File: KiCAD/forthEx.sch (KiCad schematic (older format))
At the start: 58 parts, among them CON1 SD_Card, CON2 BARREL_JACK 2,1mm, J1 RCA_JACK, J2 RCA_JACK, J3 RJ12, P1 ICSP, Q1 2N3906, Q2 2N3904, SW1 Power, SW2 reset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

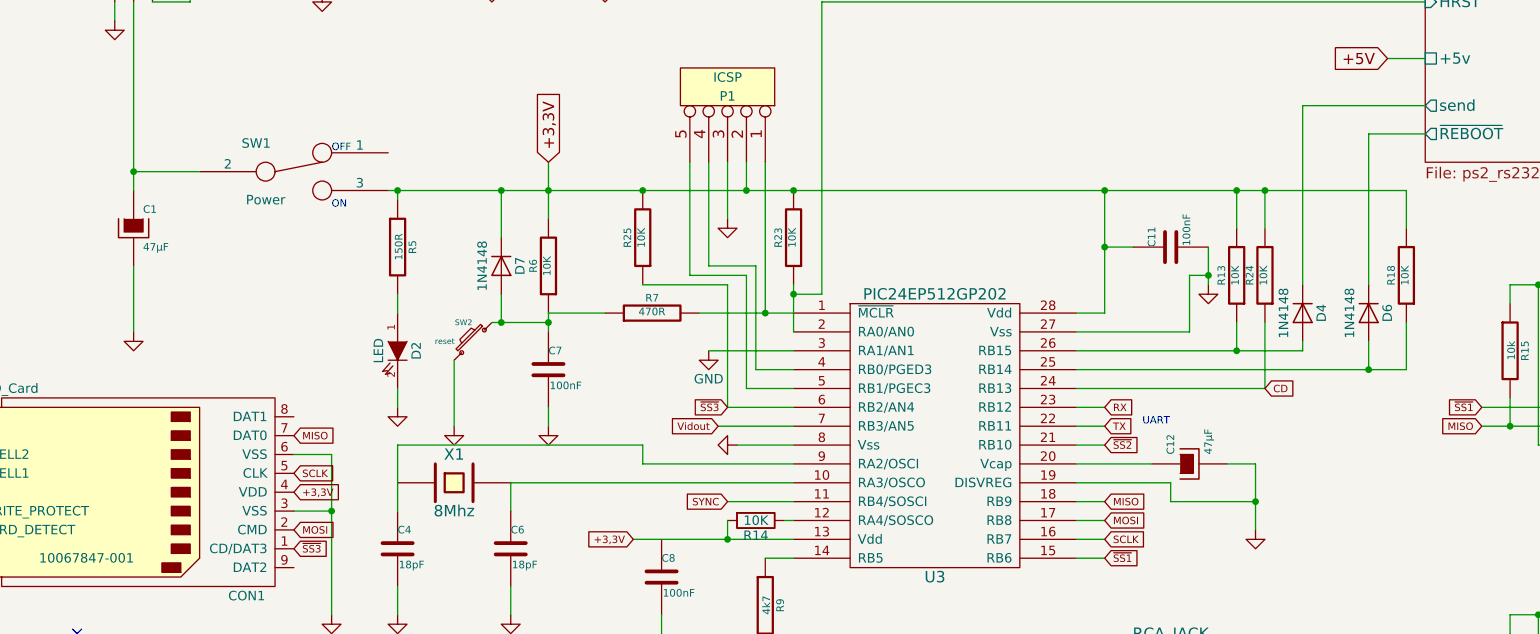
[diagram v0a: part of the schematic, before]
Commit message: Mise à jour schématique Modification à BOOT, protection contre les images passées date. Lorsque le système est mis à jour les images sauvegardées avant cette mise à jour sont invalides.
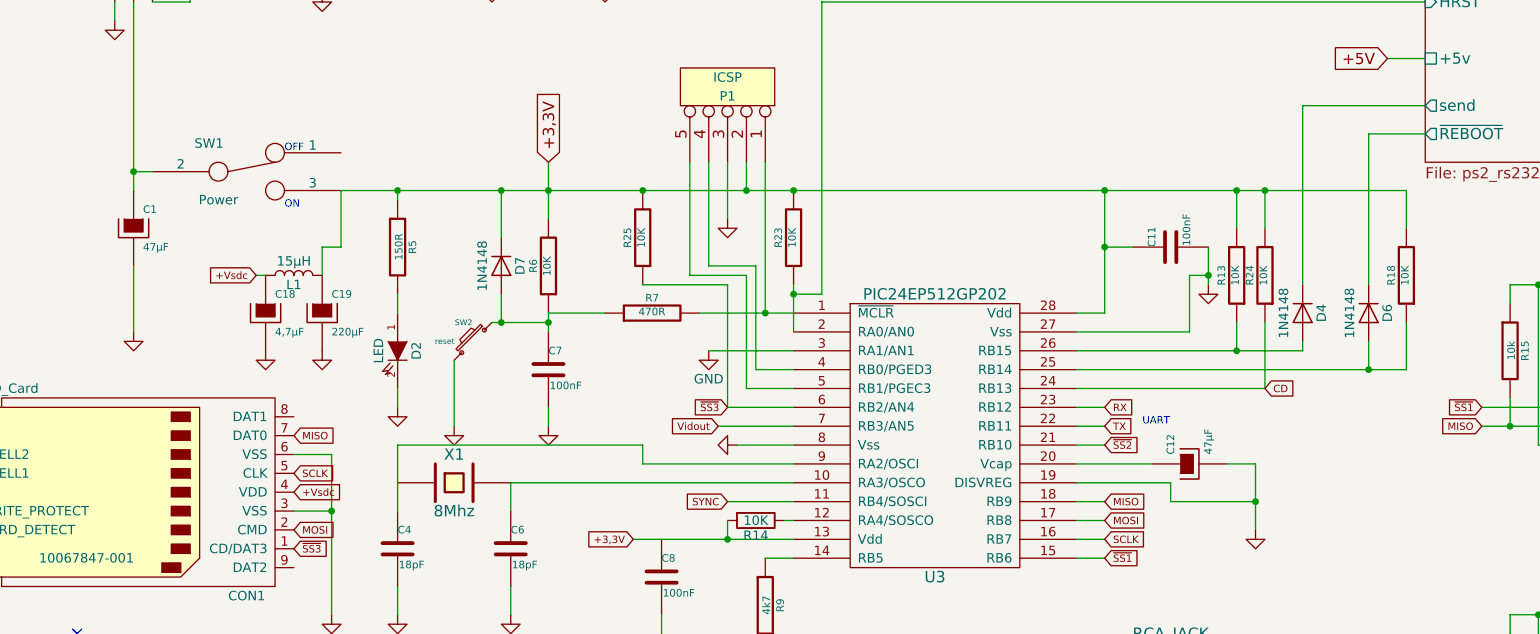
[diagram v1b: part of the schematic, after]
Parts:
- added C18: 4,7µF, ~, symbol CAPAPOL
- added C19: 220µF, ~, symbol CAPAPOL
- added L1: 15µH, symbol L
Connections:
- net +3,3V: now also C19.1, L1.2; no longer CON1.4 (VDD)
- net GND: now also C18.2, C19.2
- new net +Vsdc: C18.1, CON1.4 (VDD), L1.1
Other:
- moved on the sheet: SW1
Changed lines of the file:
@@
 $EndComp
 $Comp
-L GND #PWR23
+L GND #PWR25
 U 1 1 55772493
 P 6300 5700
-F 0 "#PWR23" H 6300 5700 30  0001 C CNN
+F 0 "#PWR25" H 6300 5700 30  0001 C CNN
 F 1 "GND" H 6300 5630 30  0001 C CNN
 F 2 "" H 6300 5700 60  0000 C CNN
@@
 $EndComp
 $Comp
-L GND #PWR22
+L GND #PWR24
 U 1 1 5577274E
 P 5950 7450
-F 0 "#PWR22" H 5950 7450 30  0001 C CNN
+F 0 "#PWR24" H 5950 7450 30  0001 C CNN
 F 1 "GND" H 5950 7380 30  0001 C CNN
 F 2 "" H 5950 7450 60  0000 C CNN
@@
 $EndComp
 $Comp
-L GND #PWR14
+L GND #PWR16
 U 1 1 55772AE7
 P 3900 3650
-F 0 "#PWR14" H 3900 3650 30  0001 C CNN
+F 0 "#PWR16" H 3900 3650 30  0001 C CNN
 F 1 "GND" H 3900 3580 30  0001 C CNN
 F 2 "" H 3900 3650 60  0000 C CNN
@@
 $EndComp
 $Comp
-L GND #PWR11
+L GND #PWR13
 U 1 1 55772AF4
 P 3400 3650
-F 0 "#PWR11" H 3400 3650 30  0001 C CNN
+F 0 "#PWR13" H 3400 3650 30  0001 C CNN
 F 1 "GND" H 3400 3580 30  0001 C CNN
 F 2 "" H 3400 3650 60  0000 C CNN
@@
 $EndComp
 $Comp
-L GND #PWR18
+L GND #PWR20
 U 1 1 55772BB1
 P 4850 2550
-F 0 "#PWR18" H 4850 2550 30  0001 C CNN
+F 0 "#PWR20" H 4850 2550 30  0001 C CNN
 F 1 "GND" H 4850 2480 30  0001 C CNN
 F 2 "" H 4850 2550 60  0000 C CNN
@@
 $EndComp
 $Comp
-L GND #PWR25
+L GND #PWR27
 U 1 1 55772ED2
 P 7400 2900
-F 0 "#PWR25" H 7400 2900 30  0001 C CNN
+F 0 "#PWR27" H 7400 2900 30  0001 C CNN
 F 1 "GND" H 7400 2830 30  0001 C CNN
 F 2 "" H 7400 2900 60  0000 C CNN
@@
 $EndComp
 $Comp
-L GND #PWR16
+L GND #PWR18
 U 1 1 55772F91
 P 4500 4750
-F 0 "#PWR16" H 4500 4750 30  0001 C CNN
+F 0 "#PWR18" H 4500 4750 30  0001 C CNN
 F 1 "GND" H 4500 4680 30  0001 C CNN
 F 2 "" H 4500 4750 60  0000 C CNN
@@
 $EndComp
 $Comp
-L GND #PWR26
+L GND #PWR28
 U 1 1 55773073
 P 7650 4200
-F 0 "#PWR26" H 7650 4200 30  0001 C CNN
+F 0 "#PWR28" H 7650 4200 30  0001 C CNN
 F 1 "GND" H 7650 4130 30  0001 C CNN
 F 2 "" H 7650 4200 60  0000 C CNN
@@
 $EndComp
 $Comp
-L GND #PWR13
+L GND #PWR15
 U 1 1 55773799
 P 3700 4650
-F 0 "#PWR13" H 3700 4650 30  0001 C CNN
+F 0 "#PWR15" H 3700 4650 30  0001 C CNN
 F 1 "GND" H 3700 4580 30  0001 C CNN
 F 2 "" H 3700 4650 60  0000 C CNN
@@
 $EndComp
 $Comp
-L GND #PWR9
+L GND #PWR11
 U 1 1 5577379F
 P 3100 4650
-F 0 "#PWR9" H 3100 4650 30  0001 C CNN
+F 0 "#PWR11" H 3100 4650 30  0001 C CNN
 F 1 "GND" H 3100 4580 30  0001 C CNN
 F 2 "" H 3100 4650 60  0000 C CNN
@@
 $EndComp
 $Comp
-L GND #PWR27
+L GND #PWR29
 U 1 1 55773979
 P 9350 4050
-F 0 "#PWR27" H 9350 4050 30  0001 C CNN
+F 0 "#PWR29" H 9350 4050 30  0001 C CNN
 F 1 "GND" H 9350 3980 30  0001 C CNN
 F 2 "" H 9350 4050 60  0000 C CNN
@@
 $EndComp
 $Comp
-L GND #PWR29
+L GND #PWR31
 U 1 1 55773B44
 P 10900 3700
-F 0 "#PWR29" H 10900 3700 30  0001 C CNN
+F 0 "#PWR31" H 10900 3700 30  0001 C CNN
 F 1 "GND" H 10900 3630 30  0001 C CNN
 F 2 "" H 10900 3700 60  0000 C CNN
@@
 L SWITCH_INV SW1
 U 1 1 55775625
-P 2550 2300
-F 0 "SW1" H 2350 2450 50  0000 C CNN
-F 1 "Power" H 2400 2150 50  0000 C CNN
-F 2 "~" H 2550 2300 60  0000 C CNN
-F 3 "~" H 2550 2300 60  0000 C CNN
-	1    2550 2300
-	1    0    0    -1
-$EndComp
-$Comp
-L GND #PWR3
+P 2300 2300
+F 0 "SW1" H 2100 2450 50  0000 C CNN
+F 1 "Power" H 2150 2150 50  0000 C CNN
+F 2 "~" H 2300 2300 60  0000 C CNN
+F 3 "~" H 2300 2300 60  0000 C CNN
+	1    2300 2300
+	1    0    0    -1
+$EndComp
+$Comp
+L GND #PWR5
 U 1 1 55775634
 P 1700 3150
-F 0 "#PWR3" H 1700 3150 30  0001 C CNN
+F 0 "#PWR5" H 1700 3150 30  0001 C CNN
 F 1 "GND" H 1700 3080 30  0001 C CNN
 F 2 "" H 1700 3150 60  0000 C CNN
@@
 $EndComp
 $Comp
-L GND #PWR19
+L GND #PWR21
 U 1 1 557795A1
 P 4900 3750
-F 0 "#PWR19" H 4900 3750 30  0001 C CNN
+F 0 "#PWR21" H 4900 3750 30  0001 C CNN
 F 1 "GND" H 4900 3680 30  0001 C CNN
 F 2 "" H 4900 3750 60  0000 C CNN
@@
 $EndComp
 $Comp
-L GND #PWR8
+L GND #PWR10
 U 1 1 557C9D8C
 P 3100 3550
-F 0 "#PWR8" H 3100 3550 30  0001 C CNN
+F 0 "#PWR10" H 3100 3550 30  0001 C CNN
 F 1 "GND" H 3100 3480 30  0001 C CNN
 F 2 "" H 3100 3550 60  0000 C CNN
@@
 $EndComp
 $Comp
-L GND #PWR2
+L GND #PWR4
 U 1 1 557CC219
 P 1600 1500
-F 0 "#PWR2" H 1600 1500 30  0001 C CNN
+F 0 "#PWR4" H 1600 1500 30  0001 C CNN
 F 1 "GND" H 1600 1430 30  0001 C CNN
 F 2 "" H 1600 1500 60  0000 C CNN
@@
 $EndComp
 $Comp
-L GND #PWR15
+L GND #PWR17
 U 1 1 557CC2EB
 P 4200 1300
-F 0 "#PWR15" H 4200 1300 30  0001 C CNN
+F 0 "#PWR17" H 4200 1300 30  0001 C CNN
 F 1 "GND" H 4200 1230 30  0001 C CNN
 F 2 "" H 4200 1300 60  0000 C CNN
@@
 	1    0    0    -1
 $EndComp
-Text Notes 2750 2500 0    39   ~ 0
+Text Notes 2500 2500 0    39   ~ 0
 ON
-Text Notes 2750 2200 0    39   ~ 0
+Text Notes 2500 2200 0    39   ~ 0
 OFF
 $Comp
@@
 $EndComp
 $Comp
-L GND #PWR24
+L GND #PWR26
 U 1 1 557CD0FD
 P 7200 5650
-F 0 "#PWR24" H 7200 5650 30  0001 C CNN
+F 0 "#PWR26" H 7200 5650 30  0001 C CNN
 F 1 "GND" H 7200 5580 30  0001 C CNN
 F 2 "" H 7200 5650 60  0000 C CNN
@@
 Vidout
 $Comp
-L GND #PWR28
+L GND #PWR30
 U 1 1 55FA1459
 P 9350 5800
-F 0 "#PWR28" H 9350 5800 30  0001 C CNN
+F 0 "#PWR30" H 9350 5800 30  0001 C CNN
 F 1 "GND" H 9350 5730 30  0001 C CNN
 F 2 "" H 9350 5800 60  0000 C CNN
@@
 $EndComp
 $Comp
-L GND #PWR30
+L GND #PWR32
 U 1 1 55FA1465
 P 10900 5450
-F 0 "#PWR30" H 10900 5450 30  0001 C CNN
+F 0 "#PWR32" H 10900 5450 30  0001 C CNN
 F 1 "GND" H 10900 5380 30  0001 C CNN
 F 2 "" H 10900 5450 60  0000 C CNN
@@
 ~SS2
 $Comp
-L GND #PWR5
+L GND #PWR7
 U 1 1 5600DB37
 P 2700 1350
-F 0 "#PWR5" H 2700 1350 30  0001 C CNN
+F 0 "#PWR7" H 2700 1350 30  0001 C CNN
 F 1 "GND" H 2700 1280 30  0001 C CNN
 F 2 "" H 2700 1350 60  0000 C CNN
@@
 $EndComp
 $Comp
-L GND #PWR21
+L GND #PWR23
 U 1 1 56014C24
 P 5950 5500
-F 0 "#PWR21" H 5950 5500 30  0001 C CNN
+F 0 "#PWR23" H 5950 5500 30  0001 C CNN
 F 1 "GND" H 5950 5430 30  0001 C CNN
 F 2 "" H 5950 5500 60  0000 C CNN
@@
 $EndComp
 $Comp
-L GND #PWR20
+L GND #PWR22
 U 1 1 56014C57
 P 5050 5500
-F 0 "#PWR20" H 5050 5500 30  0001 C CNN
+F 0 "#PWR22" H 5050 5500 30  0001 C CNN
 F 1 "GND" H 5050 5430 30  0001 C CNN
 F 2 "" H 5050 5500 60  0000 C CNN
@@
 $EndComp
 $Comp
-L GND #PWR7
+L GND #PWR9
 U 1 1 5613F3E7
 P 3050 7050
-F 0 "#PWR7" H 3050 7050 30  0001 C CNN
+F 0 "#PWR9" H 3050 7050 30  0001 C CNN
 F 1 "GND" H 3050 6980 30  0001 C CNN
 F 2 "" H 3050 7050 60  0000 C CNN
@@
 $EndComp
 $Comp
-L GND #PWR4
+L GND #PWR6
 U 1 1 5613F601
 P 1850 7400
-F 0 "#PWR4" H 1850 7400 30  0001 C CNN
+F 0 "#PWR6" H 1850 7400 30  0001 C CNN
 F 1 "GND" H 1850 7330 30  0001 C CNN
 F 2 "" H 1850 7400 60  0000 C CNN
@@
 $EndComp
 $Comp
-L GND #PWR10
+L GND #PWR12
 U 1 1 5808AF37
 P 3200 1250
-F 0 "#PWR10" H 3200 1250 30  0001 C CNN
+F 0 "#PWR12" H 3200 1250 30  0001 C CNN
 F 1 "GND" H 3200 1180 30  0001 C CNN
 F 2 "" H 3200 1250 60  0000 C CNN
@@
 CD
 $Comp
-L GND #PWR6
+L GND #PWR8
 U 1 1 5808F945
 P 2750 4650
-F 0 "#PWR6" H 2750 4650 30  0001 C CNN
+F 0 "#PWR8" H 2750 4650 30  0001 C CNN
 F 1 "GND" H 2750 4580 30  0001 C CNN
 F 2 "" H 2750 4650 60  0000 C CNN
@@
 $EndComp
 Text GLabel 2550 4000 2    39   Input ~ 0
-+3,3V
++Vsdc
 Text GLabel 4850 3550 0    39   Input ~ 0
 ~SS3
@@
 $EndComp
 $Comp
-L GND #PWR12
+L GND #PWR14
 U 1 1 5807E91E
 P 3600 1300
-F 0 "#PWR12" H 3600 1300 30  0001 C CNN
+F 0 "#PWR14" H 3600 1300 30  0001 C CNN
 F 1 "GND" H 3600 1230 30  0001 C CNN
 F 2 "" H 3600 1300 60  0000 C CNN
@@
 $EndComp
 $Comp
-L GND #PWR1
+L GND #PWR2
 U 1 1 5873C0B4
 P 1150 6050
-F 0 "#PWR1" H 1150 5800 50  0001 C CNN
+F 0 "#PWR2" H 1150 5800 50  0001 C CNN
 F 1 "GND" H 1150 5900 50  0000 C CNN
 F 2 "" H 1150 6050 50  0000 C CNN
@@
 	1700 1400 1700 2400
 Wire Wire Line
-	1700 2300 2050 2300
-Wire Wire Line
 	7200 4050 7650 4050
 Wire Wire Line
@@
 	8350 1700 8550 1700
 Wire Wire Line
-	3050 2400 8450 2400
+	2800 2400 8450 2400
 Wire Wire Line
 	7900 3250 7900 3200
@@
 	5150 4150 5200 4150
 $Comp
-L GND #PWR17
+L GND #PWR19
 U 1 1 5873EFC8
 P 4750 3250
-F 0 "#PWR17" H 4750 3000 50  0001 C CNN
+F 0 "#PWR19" H 4750 3000 50  0001 C CNN
 F 1 "GND" H 4750 3100 50  0000 C CNN
 F 2 "" H 4750 3250 50  0000 C CNN
@@
 	8450 3350 8450 3100
 Connection ~ 8250 3350
+$Comp
+L L L1
+U 1 1 58E82954
+P 2550 2850
+F 0 "L1" V 2500 2850 50  0000 C CNN
+F 1 "15µH" V 2625 2850 50  0000 C CNN
+F 2 "" H 2550 2850 50  0001 C CNN
+F 3 "" H 2550 2850 50  0001 C CNN
+	1    2550 2850
+	0    -1   -1   0
+$EndComp
+$Comp
+L CAPAPOL C18
+U 1 1 58E84A23
+P 2400 3050
+F 0 "C18" H 2450 3150 40  0000 L CNN
+F 1 "4,7µF" H 2450 2950 40  0000 L CNN
+F 2 "~" H 2500 2900 30  0000 C CNN
+F 3 "~" H 2400 3050 300 0000 C CNN
+	1    2400 3050
+	1    0    0    -1
+$EndComp
+$Comp
+L CAPAPOL C19
+U 1 1 58E84B29
+P 2700 3050
+F 0 "C19" H 2750 3150 40  0000 L CNN
+F 1 "220µF" H 2750 2950 40  0000 L CNN
+F 2 "~" H 2800 2900 30  0000 C CNN
+F 3 "~" H 2700 3050 300 0000 C CNN
+	1    2700 3050
+	1    0    0    -1
+$EndComp
+$Comp
+L GND #PWR1
+U 1 1 58E84D59
+P 2400 3250
+F 0 "#PWR1" H 2400 3250 30  0001 C CNN
+F 1 "GND" H 2400 3180 30  0001 C CNN
+F 2 "" H 2400 3250 60  0000 C CNN
+F 3 "" H 2400 3250 60  0000 C CNN
+	1    2400 3250
+	1    0    0    -1
+$EndComp
+$Comp
+L GND #PWR3
+U 1 1 58E84FE5
+P 2700 3250
+F 0 "#PWR3" H 2700 3250 30  0001 C CNN
+F 1 "GND" H 2700 3180 30  0001 C CNN
+F 2 "" H 2700 3250 60  0000 C CNN
+F 3 "" H 2700 3250 60  0000 C CNN
+	1    2700 3250
+	1    0    0    -1
+$EndComp
+Text GLabel 2350 2850 0    39   Input ~ 0
++Vsdc
+Wire Wire Line
+	2350 2850 2400 2850
+Wire Wire Line
+	2700 2850 2700 2700
+Wire Wire Line
+	1700 2300 1800 2300
+Wire Wire Line
+	2700 2700 2800 2700
+Wire Wire Line
+	2800 2700 2800 2400
 $EndSCHEMATC

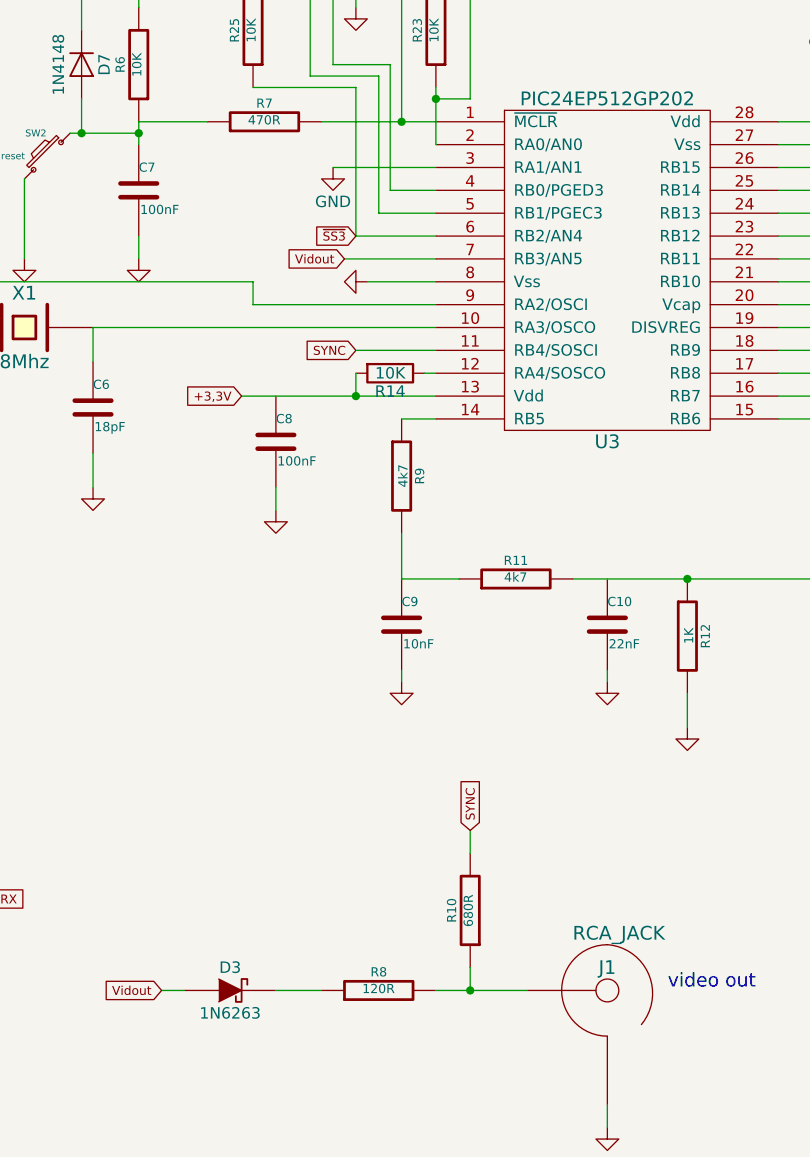
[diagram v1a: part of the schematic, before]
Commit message: Modification au générateur vidéo pour ajouter un seuil noir en utilisant OC4.
Création et travail sur block.s
Retiré eefs.s du projet.
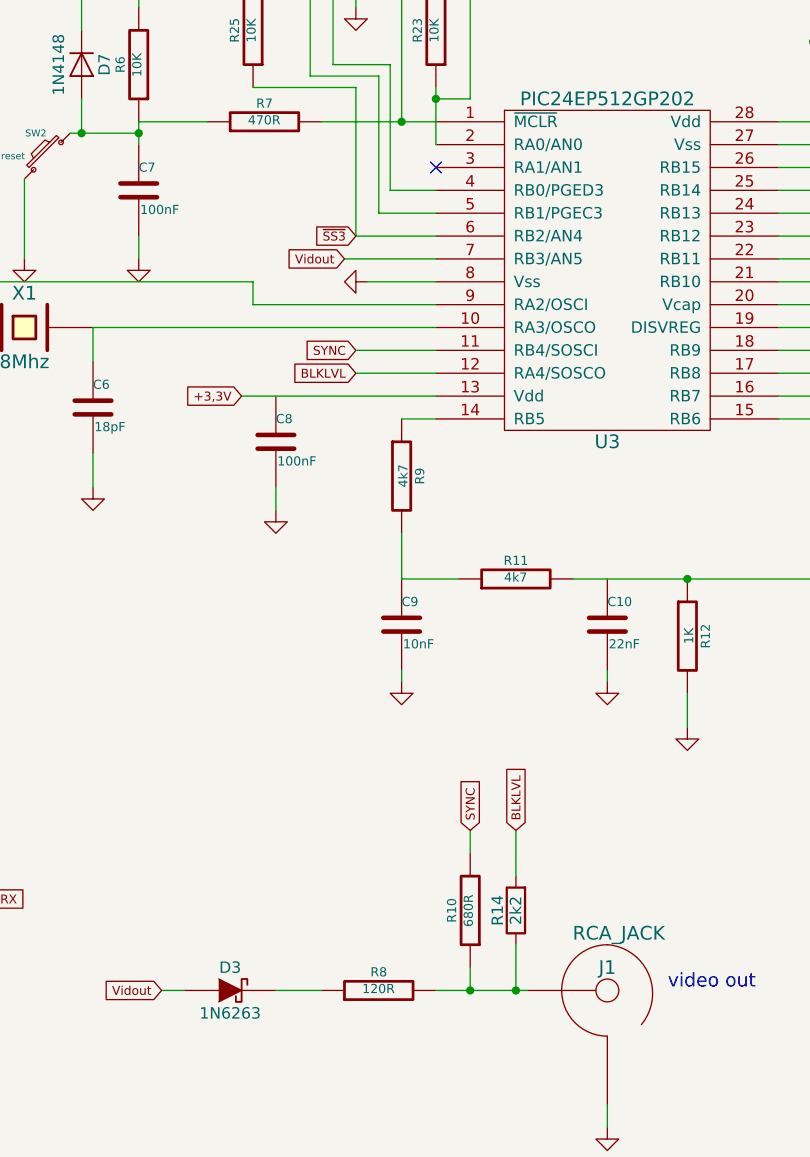
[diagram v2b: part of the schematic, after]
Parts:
- R14: value 10K -> 2k2
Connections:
- net +3,3V: no longer R14.2
- net GND: no longer U3.3 (RA1/AN1)
- net at J1.~, R10.1, R8.2: now also R14.1
- net BLKLVL: now reaches U3.12 (RA4/SOSCO)
- net BLKLVL: now also R14.2; no longer R14.1
- no-connect marks 6 -> 7
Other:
- moved on the sheet: R14
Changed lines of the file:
@@
 L R R14
 U 1 1 5873F621
-P 5000 4150
-F 0 "R14" V 5080 4150 50  0000 C CNN
-F 1 "10K" V 5000 4150 50  0000 C CNN
-F 2 "" V 4930 4150 50  0000 C CNN
-F 3 "" H 5000 4150 50  0000 C CNN
-	1    5000 4150
-	0    1    1    0
+P 5550 6500
+F 0 "R14" V 5630 6500 50  0000 C CNN
+F 1 "2k2" V 5550 6500 50  0000 C CNN
+F 2 "" V 5480 6500 50  0000 C CNN
+F 3 "" H 5550 6500 50  0000 C CNN
+	1    5550 6500
+	-1   0    0    1
 $EndComp
 Wire Wire Line
@@
 	5000 3350 5200 3350
 Wire Wire Line
-	4950 3450 5200 3450
-Wire Wire Line
 	9250 2750 9250 3000
 Wire Wire Line
@@
 	5200 6850 5600 6850
 Wire Wire Line
-	4850 4150 4850 4250
-Connection ~ 4850 4250
-Wire Wire Line
-	5150 4150 5200 4150
-$Comp
-L GND #PWR19
-U 1 1 5873EFC8
-P 4750 3250
-F 0 "#PWR19" H 4750 3000 50  0001 C CNN
-F 1 "GND" H 4750 3100 50  0000 C CNN
-F 2 "" H 4750 3250 50  0000 C CNN
-F 3 "" H 4750 3250 50  0000 C CNN
-	1    4750 3250
-	1    0    0    -1
-$EndComp
-Wire Wire Line
 	8250 2100 8550 2100
-Wire Wire Line
-	4750 3250 5200 3250
 $Comp
 L R-RESCUE-forthEx R23
@@
 Wire Wire Line
 	2800 2700 2800 2400
+NoConn ~ 5200 3250
+Wire Wire Line
+	5550 6650 5550 6850
+Connection ~ 5550 6850
+Text GLabel 5550 6150 1    39   Input ~ 0
+BLKLVL
+Wire Wire Line
+	5550 6150 5550 6350
+Text GLabel 4850 4150 0    39   Input ~ 0
+BLKLVL
+Wire Wire Line
+	4850 4150 5200 4150
+Wire Wire Line
+	4950 3450 5200 3450
 $EndSCHEMATC
